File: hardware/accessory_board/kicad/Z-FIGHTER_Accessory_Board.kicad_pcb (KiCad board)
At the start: 2 copper layers, 100 x 75 mm, 25 parts, among them J7 ST7920 Graphic LCD, J9 Conn_02x13_Odd_Even, Q1 BC337, Q2 BC337, SW1 Up (A0), SW2 Down (A1), SW3 Left (A2), SW4 Right (A3), SW5 A (A4), SW6 B (A5)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

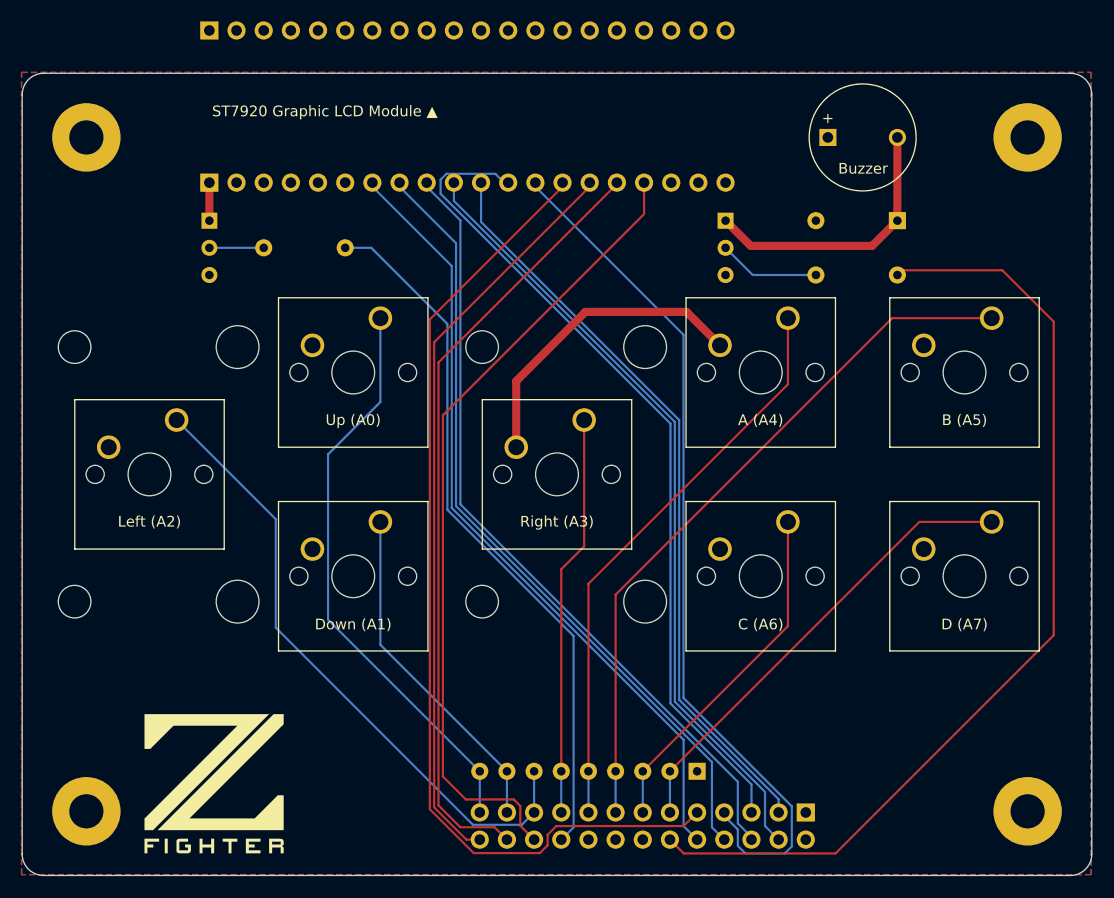
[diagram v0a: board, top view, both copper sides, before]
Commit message: Rounded corners
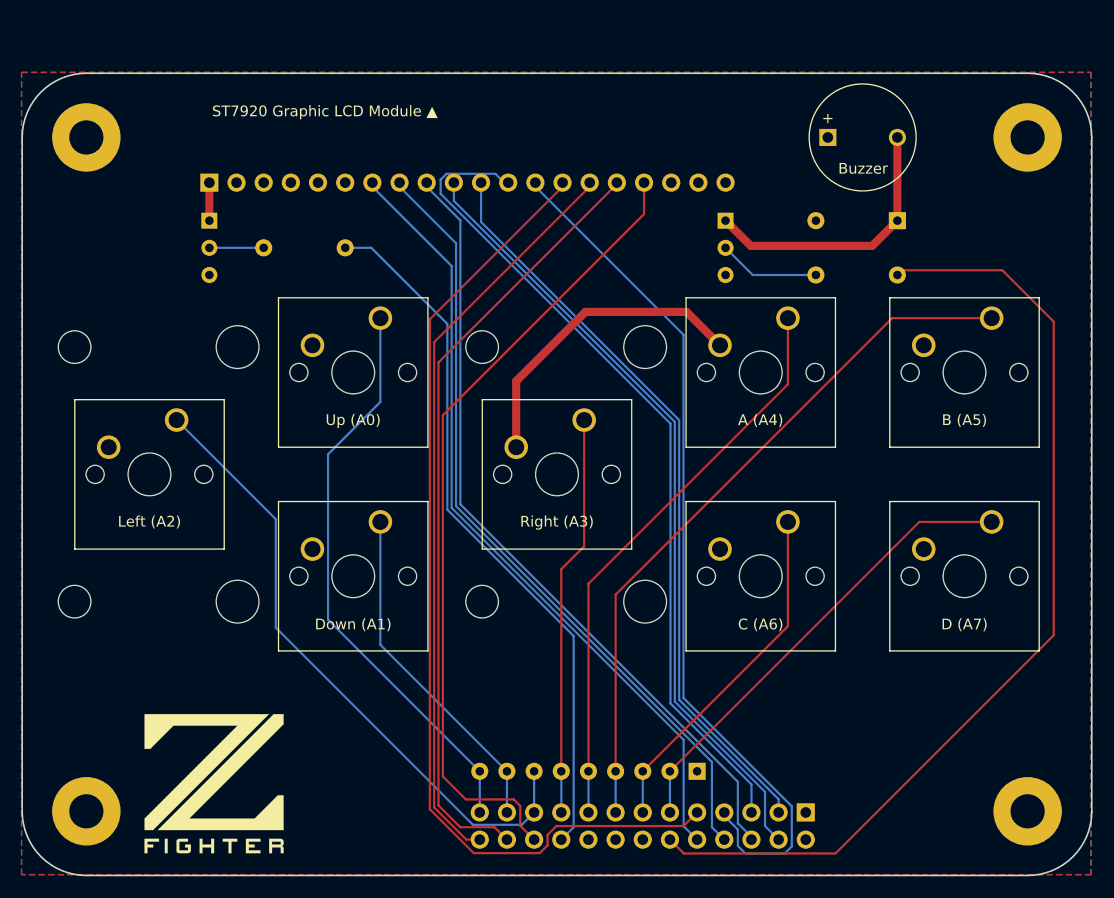
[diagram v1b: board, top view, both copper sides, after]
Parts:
- removed the J7 at (81.5, 91.0)
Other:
- outline, holes or cut-outs redrawn
- board text added: "Accessory Board Rev. 1e"
- board text removed: "Accessory Board Rev. 1d"

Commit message: Silkscreen
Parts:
- moved G*** 0.73 mm to (81.9, 160.7)
